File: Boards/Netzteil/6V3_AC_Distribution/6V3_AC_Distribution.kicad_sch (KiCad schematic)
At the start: 6 parts

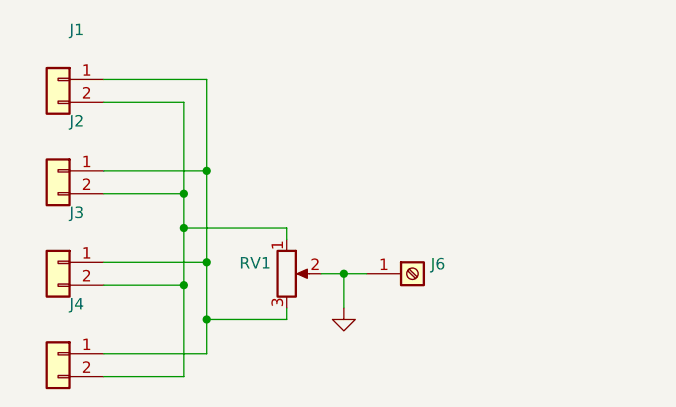
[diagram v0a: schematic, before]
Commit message: 6.3V, 400V und 400V Regler Boards bestellt
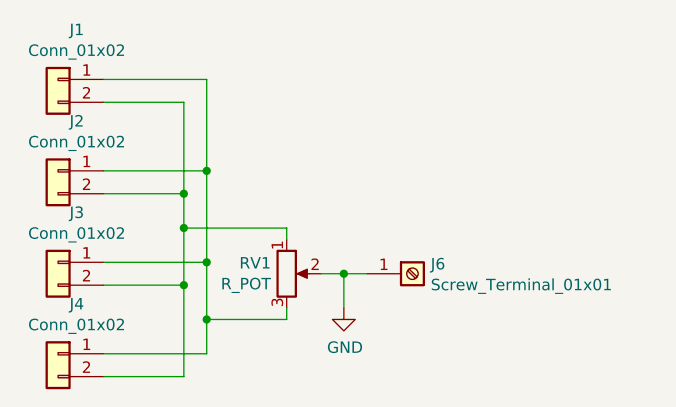
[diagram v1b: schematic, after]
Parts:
- J1, J2, J3, J4: value (none) -> Conn_01x02; footprint (none) -> Connector_TE-Connectivity:TE_MATE-N-LOK_1-770866-x_1x02_P4.14mm_Vertical
- J6: value (none) -> Screw_Terminal_01x01; footprint (none) -> MountingHole:MountingHole_3.2mm_M3_DIN965_Pad_TopOnly
- RV1: value (none) -> R_POT; footprint (none) -> Potentiometer_THT:Potentiometer_Piher_PT-10-V10_Vertical

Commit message: Leiterplatte erstellt
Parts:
- J1, J2, J3, J4: footprint Connector_TE-Connectivity:TE_MATE-N-LOK_1-770866-x_1x02_P4.14mm_Vertical -> Connector_Molex:Molex_Mini-Fit_Jr_5566-02A_2x01_P4.20mm_Vertical
- RV1: footprint Potentiometer_THT:Potentiometer_Piher_PT-10-V10_Vertical -> Potentiometer_THT:Potentiometer_Piher_PT-15-V02_Vertical
